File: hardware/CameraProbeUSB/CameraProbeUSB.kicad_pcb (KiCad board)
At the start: 2 copper layers, 75.3 x 28 mm, 42 parts, among them J1 USB-A plug (IN), J2 USB-A socket (OUT), Q1 MMBT3904, Q2 MMBT3904, Q3 AO3401A, Q4 2N7002, SW1 Button, U1 AMS1117-3.3, U2 CH340C, U3 ESP-12F

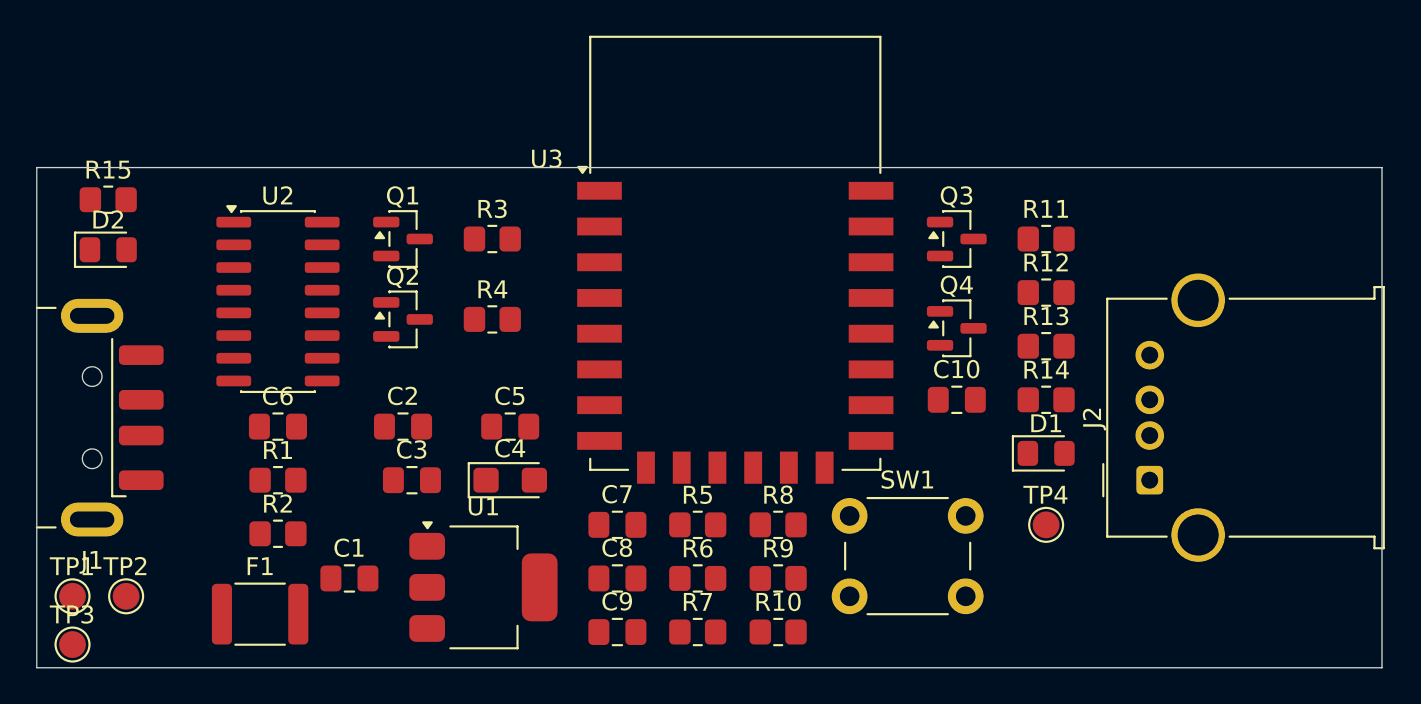
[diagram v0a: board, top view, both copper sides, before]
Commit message: Rev A board routed (Freerouting), DRC clean except silkscreen
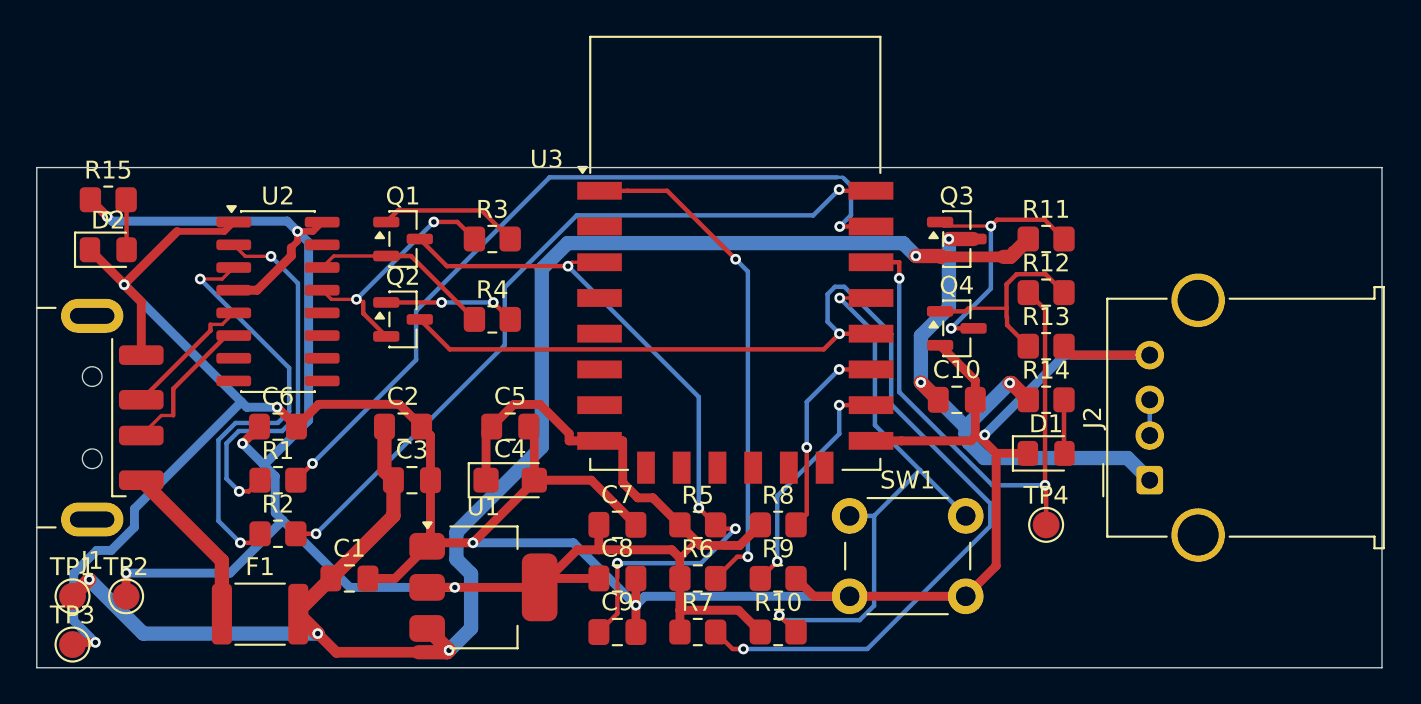
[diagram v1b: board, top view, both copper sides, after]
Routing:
- net /GND: track 0.00 -> 159.4 mm, vias 0 -> 6
- net /+3V3: track 0.00 -> 117.5 mm, vias 0 -> 5
- net /+5V: track 0.00 -> 92.1 mm, vias 0 -> 4
- net /GPIO0: track 0.00 -> 65.3 mm, vias 0 -> 2
- net /ESP_RXD: track 0.00 -> 44.2 mm, vias 0 -> 2
- net /ESP_TXD: track 0.00 -> 42.1 mm, vias 0 -> 2
- net /EN: track 0.00 -> 41.6 mm, vias 0 -> 4
- net /BTN: track 0.00 -> 34.0 mm, vias 0 -> 2
- net /SW_DRV: track 0.00 -> 32.6 mm, vias 0 -> 2
- net /5V_OUT: track 0.00 -> 31.8 mm, vias 0 -> 3
- net /RST: track 0.00 -> 28.5 mm, vias 0 -> 2
- net /CH_RXD: track 0.00 -> 23.8 mm, vias 0 -> 2
- net /CH_TXD: track 0.00 -> 20.9 mm, vias 0 -> 2
- net /Q3_G: track 0.00 -> 15.5 mm, vias 0 -> 2
- net /DTR: track 0.00 -> 13.9 mm, vias 0 -> 2
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
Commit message: Silkscreen cleanup, back labels, assembly map
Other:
- board text added: "CameraProbe USB Rev A"
- board text added: "IN"
- board text added: "OUT"
- board text added: "W9TIM / github.com/W9TIM/CameraProbe"
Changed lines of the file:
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@@
 			(at 0 -1.75 0)
 			(layer "F.SilkS")
+			(hide yes)
 			(effects
 				(font
@@
 			(at 0 -1.65 0)
 			(layer "F.SilkS")
+			(hide yes)
 			(effects
 				(font
@@
 			(at 0 -1.65 0)
 			(layer "F.SilkS")
+			(hide yes)
 			(effects
 				(font
@@
 			(at 0 -1.65 0)
 			(layer "F.SilkS")
+			(hide yes)
 			(effects
 				(font
@@
 			(at 0 -1.65 0)
 			(layer "F.SilkS")
+			(hide yes)
 			(effects
 				(font
@@
 			(at 0 -1.68 0)
 			(layer "F.SilkS")
+			(hide yes)
 			(effects
 				(font
@@
 			(at 0 -1.65 0)
 			(layer "F.SilkS")
+			(hide yes)
 			(effects
 				(font
@@
 			(at 0 -1.68 0)
 			(layer "F.SilkS")
+			(hide yes)
 			(effects
 				(font
@@
 			(at 0 -1.648 0)
 			(layer "F.SilkS")
+			(hide yes)
 			(effects
 				(font
@@
 			(at 0 -1.65 0)
 			(layer "F.SilkS")
+			(hide yes)
 			(effects
 				(font
@@
 			(at 0 -2.4 0)
 			(layer "F.SilkS")
+			(hide yes)
 			(effects
 				(font
@@
 			(at 0 -1.65 0)
 			(layer "F.SilkS")
+			(hide yes)
 			(effects
 				(font
@@
 			(at 0 -1.65 0)
 			(layer "F.SilkS")
+			(hide yes)
 			(effects
 				(font
@@
 			(at 0 -1.68 0)
 			(layer "F.SilkS")
+			(hide yes)
 			(effects
 				(font
@@
 			(at 0 -1.648 0)
 			(layer "F.SilkS")
+			(hide yes)
 			(effects
 				(font
@@
 			(at 0 -1.648 0)
 			(layer "F.SilkS")
+			(hide yes)
 			(effects
 				(font
@@
 			(at 0 -1.65 0)
 			(layer "F.SilkS")
+			(hide yes)
 			(effects
 				(font
@@
 			(at 0 -1.68 0)
 			(layer "F.SilkS")
+			(hide yes)
 			(effects
 				(font
@@
 			(at 0 -1.68 0)
 			(layer "F.SilkS")
+			(hide yes)
 			(effects
 				(font
@@
 			(at 0 -2.4 0)
 			(layer "F.SilkS")
+			(hide yes)
 			(effects
 				(font
@@
 			(at 0 -5.9 0)
 			(layer "F.SilkS")
+			(hide yes)
 			(effects
 				(font
@@
 			(at 0 -1.65 0)
 			(layer "F.SilkS")
+			(hide yes)
 			(effects
 				(font
@@
 			(at 0 -1.68 0)
 			(layer "F.SilkS")
+			(hide yes)
 			(effects
 				(font
@@
 			(at 0 -1.65 0)
 			(layer "F.SilkS")
+			(hide yes)
 			(effects
 				(font
@@
 			(at 0 -2.65 0)
 			(layer "F.SilkS")
+			(hide yes)
 			(effects
 				(font
@@
 			(at 0 -1.65 0)
 			(layer "F.SilkS")
+			(hide yes)
 			(effects
 				(font
@@
 			(at 3.25 -2 0)
 			(layer "F.SilkS")
+			(hide yes)
 			(effects
 				(font
@@
 			(at 0 -1.65 0)
 			(layer "F.SilkS")
+			(hide yes)
 			(effects
 				(font
@@
 			(at 0 -1.68 0)
 			(layer "F.SilkS")
+			(hide yes)
 			(effects
 				(font
@@
 			(at 0 -1.68 0)
 			(layer "F.SilkS")
+			(hide yes)
 			(effects
 				(font
@@
 			(at 0 -1.65 0)
 			(layer "F.SilkS")
+			(hide yes)
 			(effects
 				(font
@@
 			(at 0 -2.4 0)
 			(layer "F.SilkS")
+			(hide yes)
 			(effects
 				(font
@@
 			(at -10.56 -5.26 0)
 			(layer "F.SilkS")
+			(hide yes)
 			(effects
 				(font
@@
 			(at 0 -1.65 0)
 			(layer "F.SilkS")
+			(hide yes)
 			(effects
 				(font
@@
 			(at -6.9 -8 180)
 			(layer "F.SilkS")
+			(hide yes)
 			(effects
 				(font
@@
 			(at 0 -1.65 0)
 			(layer "F.SilkS")
+			(hide yes)
 			(effects
 				(font
@@
 			(at 3.5 -3.19 90)
 			(layer "F.SilkS")
+			(hide yes)
 			(effects
 				(font
@@
 			(at 0 -1.68 0)
 			(layer "F.SilkS")
+			(hide yes)
 			(effects
 				(font
@@
 			(at 0 -1.648 0)
 			(layer "F.SilkS")
+			(hide yes)
 			(effects
 				(font
@@
 			(at 0 -1.65 0)
 			(layer "F.SilkS")
+			(hide yes)
 			(effects
 				(font
@@
 			(at 0 -2.4 0)
 			(layer "F.SilkS")
+			(hide yes)
 			(effects
 				(font
@@
 			(at 0 -4.5 0)
 			(layer "F.SilkS")
+			(hide yes)
 			(effects
 				(font
@@
 	)
 	(embedded_fonts no)
+	(gr_text "IN"
+		(at 103.5 102.6 0)
+		(layer "B.SilkS")
+		(effects
+			(font
+				(size 1.5 1.5)
+				(thickness 0.225)
+			)
+			(justify mirror)
+		)
+	)
+	(gr_text "OUT"
+		(at 170.0 102.6 0)
+		(layer "B.SilkS")
+		(effects
+			(font
+				(size 1.5 1.5)
+				(thickness 0.225)
+			)
+			(justify mirror)
+		)
+	)
+	(gr_text "CameraProbe USB  Rev A"
+		(at 131 124.6 0)
+		(layer "B.SilkS")
+		(effects
+			(font
+				(size 1.2 1.2)
+				(thickness 0.18)
+			)
+			(justify mirror)
+		)
+	)
+	(gr_text "W9TIM / github.com/W9TIM/CameraProbe"
+		(at 137.5 126.6 0)
+		(layer "B.SilkS")
+		(effects
+			(font
+				(size 0.9 0.9)
+				(thickness 0.135)
+			)
+			(justify mirror)
+		)
+	)
 )
